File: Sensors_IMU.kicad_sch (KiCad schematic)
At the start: 19 parts, among them U19 ICM-20948, U20 KXTJ3-1057, U24 KX023-1025, U6 LSM303AH

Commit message: WIP: remove unneeded parts from PCB, add SPA06 and FHTC3 to schematics
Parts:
- C21, C22, C38, C47, C48, C49, C50, R36, R52, U19, U24, U6: now not fitted; now left out of the parts list
- R35, R53: now left out of the parts list

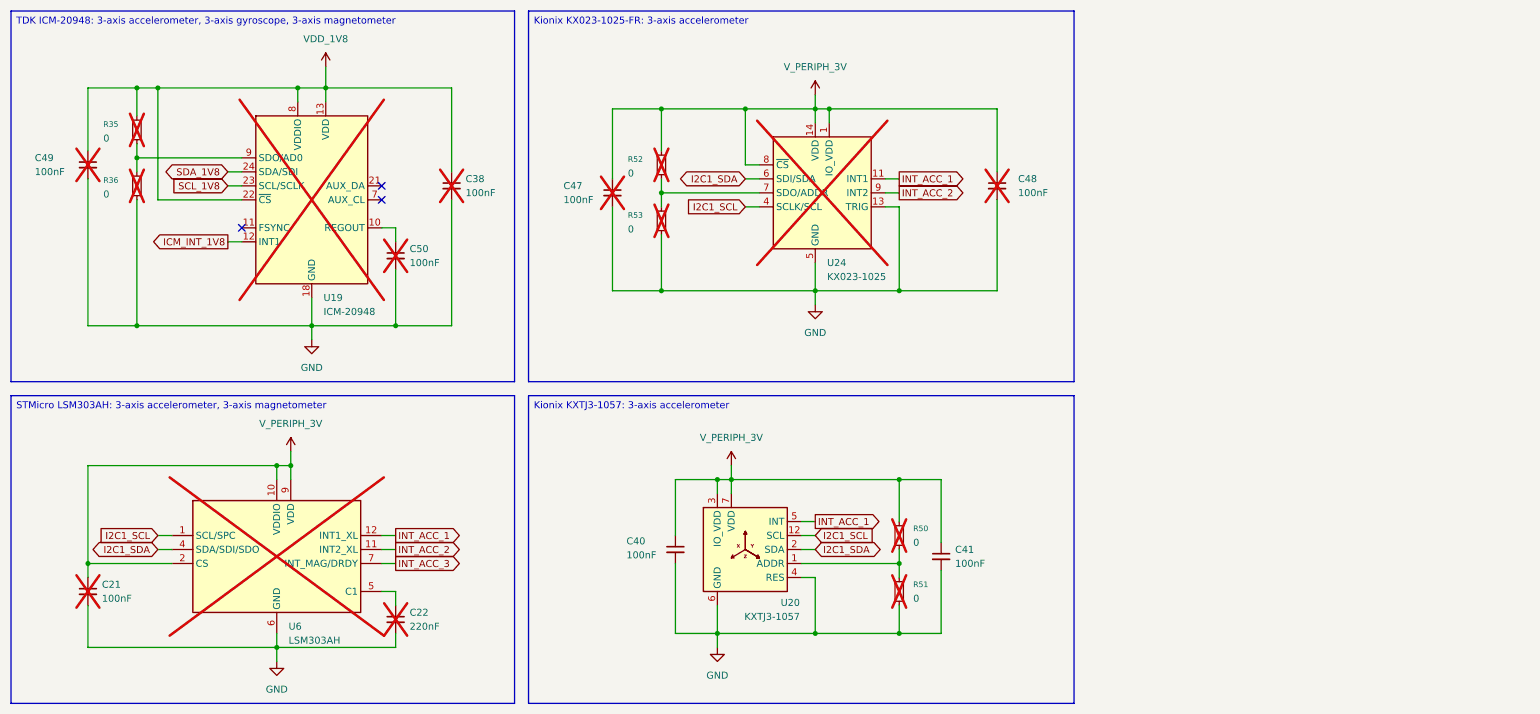
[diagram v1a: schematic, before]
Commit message: WIP: import ambient-pcb-lifepo4protection and ambient-pcb-audiopower schematics
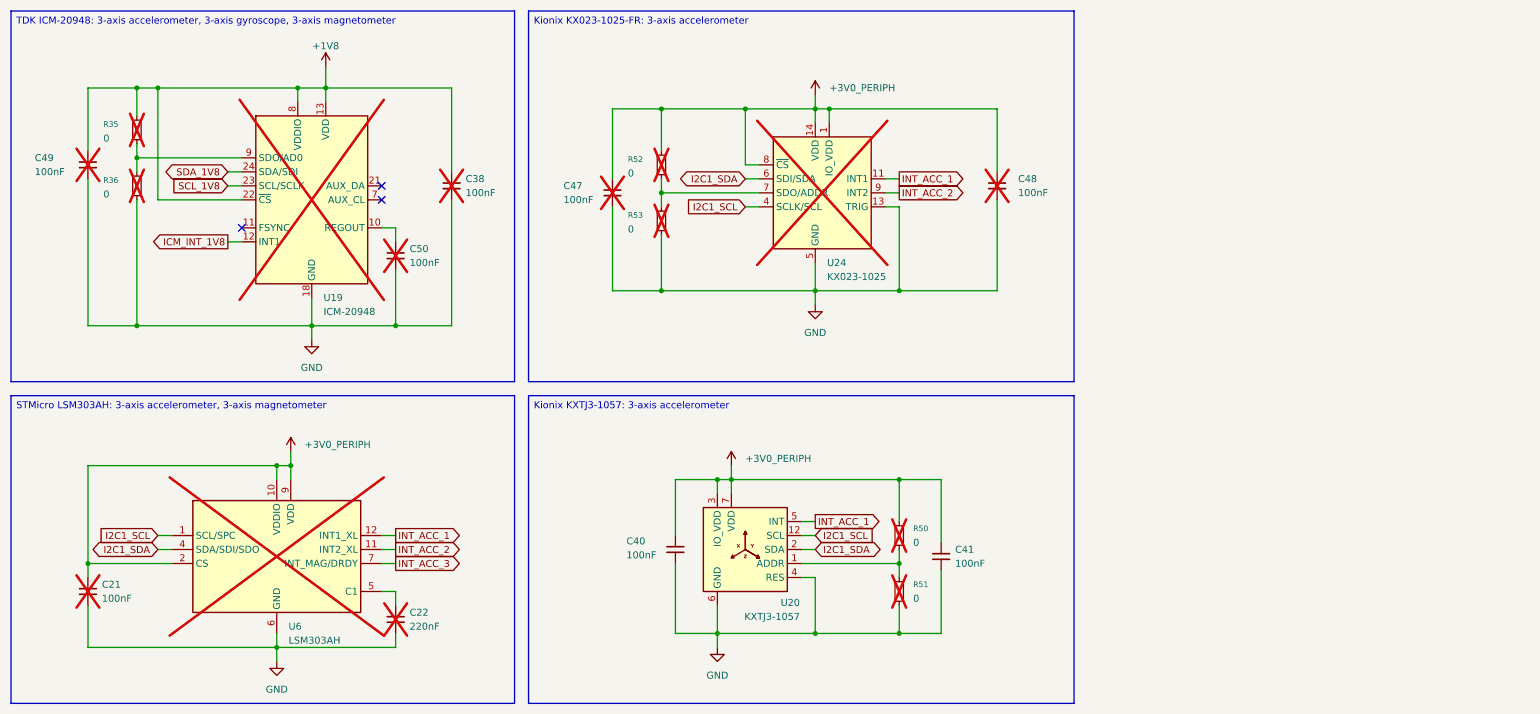
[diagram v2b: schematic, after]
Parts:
- C21, C22, C38, C47, C48, C49, C50: now in the parts list
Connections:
- net VDD_1V8 renamed +1V8
- net V_PERIPH_3V renamed +3V0_PERIPH

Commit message: WIP: BOM
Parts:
- added C115: 100nF, Capacitor_SMD:C_0402_1005Metric, symbol Device:C_Small
- added R85, R86: 0, Resistor_SMD:R_0402_1005Metric, symbol Device:R_Small
- added U45: LSM6DS3TR-C, Package_LGA:LGA-14_3x2.5mm_P0.5mm_LayoutBorder3x4y, symbol Sensor_Motion:LSM6DS3
- C21, C38, C47, C48, C49, C50: LCSC (none) -> C1525; now left out of the parts list
- C22: LCSC (none) -> C16772; now left out of the parts list
- C40, C41: LCSC (none) -> C1525; now not fitted; now left out of the parts list
- R35, R36, R52, R53: LCSC (none) -> C17168
- R50, R51: LCSC (none) -> C17168; now left out of the parts list
- U20: now not fitted; now left out of the parts list
- U24: LCSC (none) -> C236128
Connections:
- net +3V0_PERIPH: now also C115.1, R85.1, U45.12 (CS), U45.5 (VDDIO), U45.8 (VDD)
- net GND: now also C115.2, R86.2, U45.2 (SDX), U45.3 (SCX), U45.6 (GND), U45.7 (GND)
- net I2C1_SCL: now also U45.13 (SCL)
- net I2C1_SDA: now also U45.14 (SDA)
- net INT_ACC_1: now also U45.4 (INT1)
- net INT_ACC_2: now also U45.9 (INT2)
- new net: R85.2, R86.1, U45.1 (SDO/SA0)
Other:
- moved on the sheet: C21, C22, C38, C47, C48, C49, C50, R35, R36, R50, R51, R52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
